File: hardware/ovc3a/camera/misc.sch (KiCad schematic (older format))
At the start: 2 parts, among them CON1 microSD_Card, U9 ARJ11C-MBSAS-A-BA-7MU2

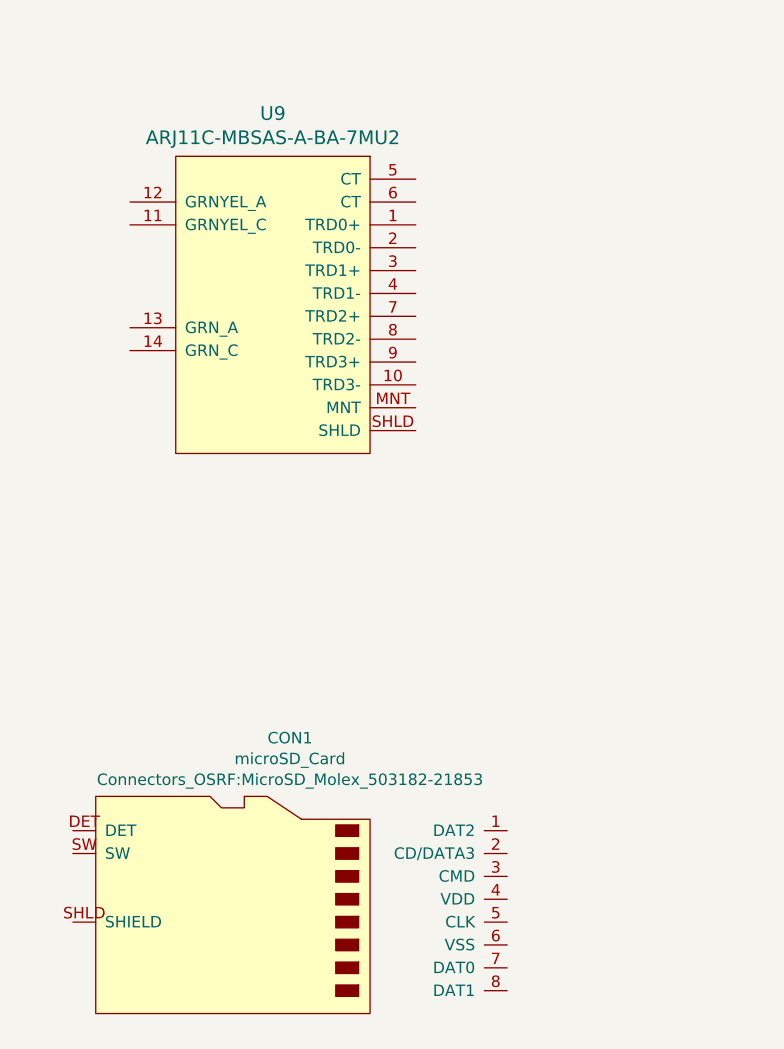
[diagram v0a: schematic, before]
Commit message: Shifted TE0820 module to make space for connectors, fixed library paths
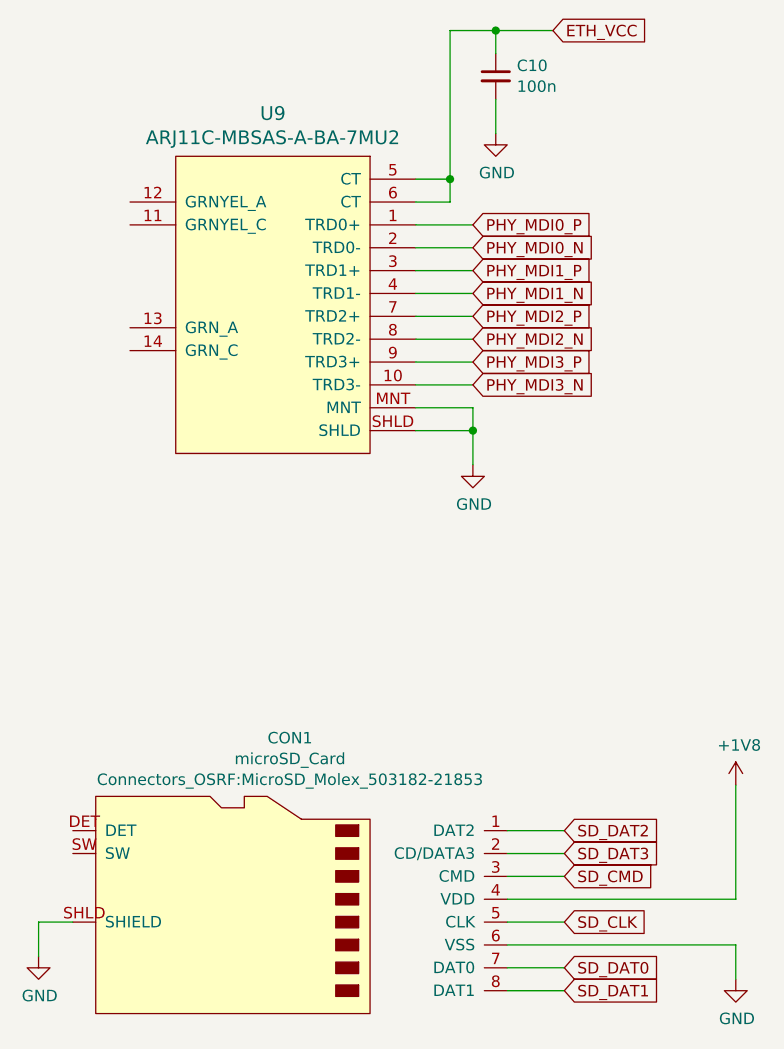
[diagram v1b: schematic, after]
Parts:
- added C10: 100n, Capacitor_SMD:C_0402_1005Metric, symbol Device:C_Small
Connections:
- net SD_DAT2: now reaches CON1.1 (DAT2)
- net SD_DAT3: now reaches CON1.2 (CD/DATA3)
- net SD_CMD: now reaches CON1.3 (CMD)
- net +1V8: now reaches CON1.4 (VDD)
- net SD_CLK: now reaches CON1.5 (CLK)
- net GND: now reaches CON1.6 (VSS)
- net GND: now also CON1.SHLD (SHIELD), U9.MNT, U9.SHLD, C10.2
- net SD_DAT0: now reaches CON1.7 (DAT0)
- net SD_DAT1: now reaches CON1.8 (DAT1)
- net PHY_MDI0_P: now reaches U9.1 (TRD0+)
- net PHY_MDI3_N: now reaches U9.10 (TRD3-)
- net PHY_MDI0_N: now reaches U9.2 (TRD0-)
- net PHY_MDI1_P: now reaches U9.3 (TRD1+)
- net PHY_MDI1_N: now reaches U9.4 (TRD1-)
- net ETH_VCC: now reaches U9.5 (CT)
- net ETH_VCC: now also U9.6 (CT), C10.1
- net PHY_MDI2_P: now reaches U9.7 (TRD2+)
- net PHY_MDI2_N: now reaches U9.8 (TRD2-)
- net PHY_MDI3_P: now reaches U9.9 (TRD3+)
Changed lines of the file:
@@
 	1    0    0    -1
 $EndComp
+Wire Wire Line
+	3050 1800 3300 1800
+Wire Wire Line
+	3300 1900 3050 1900
+Wire Wire Line
+	3300 2100 3050 2100
+Wire Wire Line
+	3050 2000 3300 2000
+Wire Wire Line
+	3300 2200 3050 2200
+Wire Wire Line
+	3050 2300 3300 2300
+Wire Wire Line
+	3300 2400 3050 2400
+Wire Wire Line
+	3050 2500 3300 2500
+$Comp
+L Device:C_Small C10
+U 1 1 5C4844F8
+P 3400 1150
+F 0 "C10" H 3492 1196 50  0000 L CNN
+F 1 "100n" H 3492 1105 50  0000 L CNN
+F 2 "Capacitor_SMD:C_0402_1005Metric" H 3400 1150 50  0001 C CNN
+F 3 "~" H 3400 1150 50  0001 C CNN
+	1    3400 1150
+	1    0    0    -1
+$EndComp
+Wire Wire Line
+	3050 1600 3200 1600
+Wire Wire Line
+	3200 1600 3200 950
+Wire Wire Line
+	3200 950  3400 950
+Wire Wire Line
+	3400 950  3400 1050
+Wire Wire Line
+	3050 1700 3200 1700
+Wire Wire Line
+	3200 1700 3200 1600
+Connection ~ 3200 1600
+$Comp
+L power:GND #PWR0115
+U 1 1 5C4874B9
+P 3400 1400
+F 0 "#PWR0115" H 3400 1150 50  0001 C CNN
+F 1 "GND" H 3405 1227 50  0000 C CNN
+F 2 "" H 3400 1400 50  0001 C CNN
+F 3 "" H 3400 1400 50  0001 C CNN
+	1    3400 1400
+	1    0    0    -1
+$EndComp
+$Comp
+L power:GND #PWR0116
+U 1 1 5C48A3ED
+P 3300 2850
+F 0 "#PWR0116" H 3300 2600 50  0001 C CNN
+F 1 "GND" H 3305 2677 50  0000 C CNN
+F 2 "" H 3300 2850 50  0001 C CNN
+F 3 "" H 3300 2850 50  0001 C CNN
+	1    3300 2850
+	1    0    0    -1
+$EndComp
+Wire Wire Line
+	3050 2700 3300 2700
+Wire Wire Line
+	3300 2700 3300 2850
+Wire Wire Line
+	3050 2600 3300 2600
+Wire Wire Line
+	3300 2600 3300 2700
+Connection ~ 3300 2700
+Wire Wire Line
+	3400 1400 3400 1250
+Wire Wire Line
+	3700 4450 3450 4450
+Wire Wire Line
+	3700 4550 3450 4550
+Wire Wire Line
+	3700 4650 3450 4650
+Wire Wire Line
+	3700 5150 3450 5150
+Wire Wire Line
+	3700 5050 3450 5050
+Wire Wire Line
+	3700 4850 3450 4850
+$Comp
+L power:GND #PWR0117
+U 1 1 5C49A0AD
+P 4450 5100
+F 0 "#PWR0117" H 4450 4850 50  0001 C CNN
+F 1 "GND" H 4455 4927 50  0000 C CNN
+F 2 "" H 4450 5100 50  0001 C CNN
+F 3 "" H 4450 5100 50  0001 C CNN
+	1    4450 5100
+	1    0    0    -1
+$EndComp
+Wire Wire Line
+	3450 4750 4450 4750
+Wire Wire Line
+	3450 4950 4450 4950
+Wire Wire Line
+	4450 4950 4450 5100
+$Comp
+L power:GND #PWR0119
+U 1 1 5C49BFA5
+P 1400 5000
+F 0 "#PWR0119" H 1400 4750 50  0001 C CNN
+F 1 "GND" H 1405 4827 50  0000 C CNN
+F 2 "" H 1400 5000 50  0001 C CNN
+F 3 "" H 1400 5000 50  0001 C CNN
+	1    1400 5000
+	1    0    0    -1
+$EndComp
+Wire Wire Line
+	1550 4850 1400 4850
+Wire Wire Line
+	1400 4850 1400 5000
+Wire Wire Line
+	4450 4250 4450 4750
+$Comp
+L power:+1V8 #PWR0118
+U 1 1 5C49AC58
+P 4450 4250
+F 0 "#PWR0118" H 4450 4100 50  0001 C CNN
+F 1 "+1V8" H 4465 4423 50  0000 C CNN
+F 2 "" H 4450 4250 50  0001 C CNN
+F 3 "" H 4450 4250 50  0001 C CNN
+	1    4450 4250
+	1    0    0    -1
+$EndComp
+Text GLabel 3700 4450 2    50   Input ~ 0
+SD_DAT2
+Text GLabel 3700 4550 2    50   Input ~ 0
+SD_DAT3
+Text GLabel 3700 4650 2    50   Input ~ 0
+SD_CMD
+Text GLabel 3700 4850 2    50   Input ~ 0
+SD_CLK
+Text GLabel 3700 5050 2    50   Input ~ 0
+SD_DAT0
+Text GLabel 3700 5150 2    50   Input ~ 0
+SD_DAT1
+Text GLabel 3300 1800 2    50   Input ~ 0
+PHY_MDI0_P
+Text GLabel 3300 1900 2    50   Input ~ 0
+PHY_MDI0_N
+Text GLabel 3300 2000 2    50   Input ~ 0
+PHY_MDI1_P
+Text GLabel 3300 2100 2    50   Input ~ 0
+PHY_MDI1_N
+Text GLabel 3300 2200 2    50   Input ~ 0
+PHY_MDI2_P
+Text GLabel 3300 2300 2    50   Input ~ 0
+PHY_MDI2_N
+Text GLabel 3300 2400 2    50   Input ~ 0
+PHY_MDI3_P
+Text GLabel 3300 2500 2    50   Input ~ 0
+PHY_MDI3_N
+Text GLabel 3650 950  2    50   Input ~ 0
+ETH_VCC
+Wire Wire Line
+	3650 950  3400 950
+Connection ~ 3400 950
 $EndSCHEMATC

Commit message: Fixed SD power to 3.3V
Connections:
- net +1V8 renamed +3V3
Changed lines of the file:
@@
 Wire Wire Line
 	4450 4250 4450 4750
-$Comp
-L power:+1V8 #PWR0118
-U 1 1 5C49AC58
-P 4450 4250
-F 0 "#PWR0118" H 4450 4100 50  0001 C CNN
-F 1 "+1V8" H 4465 4423 50  0000 C CNN
-F 2 "" H 4450 4250 50  0001 C CNN
-F 3 "" H 4450 4250 50  0001 C CNN
-	1    4450 4250
-	1    0    0    -1
-$EndComp
 Text GLabel 3700 4450 2    50   Input ~ 0
 SD_DAT2
@@
 	3650 950  3400 950
 Connection ~ 3400 950
+$Comp
+L power:+3.3V #PWR?
+U 1 1 5C4E6A5A
+P 4450 4250
+F 0 "#PWR?" H 4450 4100 50  0001 C CNN
+F 1 "+3.3V" H 4465 4423 50  0000 C CNN
+F 2 "" H 4450 4250 50  0001 C CNN
+F 3 "" H 4450 4250 50  0001 C CNN
+	1    4450 4250
+	1    0    0    -1
+$EndComp
 $EndSCHEMATC

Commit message: Preliminary component placement
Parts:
- added J5: Conn_02x15_Odd_Even, Connector_PinHeader_2.00mm:PinHeader_2x15_P2.00mm_Vertical, symbol Connector_Generic:Conn_02x15_Odd_Even
- added R12, R13: 220R, Resistor_SMD:R_0603_1608Metric, symbol Device:R_Small
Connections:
- net +3V3: now also J5.1 (Pin_1), J5.2 (Pin_2)
- net GND: now also U9.11 (GRNYEL_C), U9.14 (GRN_C), J5.17 (Pin_17), J5.18 (Pin_18), J5.29 (Pin_29), J5.30 (Pin_30), J5.5 (Pin_5), J5.6 (Pin_6)
- net at U9.12 (GRNYEL_A): now also R12.1
- net at U9.13 (GRN_A): now also R13.1
- new net +1V8: J5.3 (Pin_3), J5.4 (Pin_4)
- new net LED_L: R13.2
- new net LED_R: R12.2
- new net PGOOD: J5.7 (Pin_7)
- new net SPI_CLK: J5.25 (Pin_25)
- new net SPI_MISO: J5.26 (Pin_26)
- new net SPI_MOSI: J5.28 (Pin_28)
- new net SPI_SS1: J5.27 (Pin_27)
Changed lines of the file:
@@
 Connection ~ 3400 950
 $Comp
-L power:+3.3V #PWR?
+L power:+3.3V #PWR0118
 U 1 1 5C4E6A5A
 P 4450 4250
-F 0 "#PWR?" H 4450 4100 50  0001 C CNN
+F 0 "#PWR0118" H 4450 4100 50  0001 C CNN
 F 1 "+3.3V" H 4465 4423 50  0000 C CNN
 F 2 "" H 4450 4250 50  0001 C CNN
@@
 	1    0    0    -1
 $EndComp
+$Comp
+L Device:R_Small R13
+U 1 1 5C4E7858
+P 1500 2250
+F 0 "R13" V 1304 2250 50  0000 C CNN
+F 1 "220R" V 1395 2250 50  0000 C CNN
+F 2 "Resistor_SMD:R_0603_1608Metric" H 1500 2250 50  0001 C CNN
+F 3 "~" H 1500 2250 50  0001 C CNN
+	1    1500 2250
+	0    1    1    0
+$EndComp
+Wire Wire Line
+	1800 2250 1600 2250
+$Comp
+L power:GND #PWR0120
+U 1 1 5C4E8986
+P 1700 2500
+F 0 "#PWR0120" H 1700 2250 50  0001 C CNN
+F 1 "GND" H 1705 2327 50  0000 C CNN
+F 2 "" H 1700 2500 50  0001 C CNN
+F 3 "" H 1700 2500 50  0001 C CNN
+	1    1700 2500
+	1    0    0    -1
+$EndComp
+Wire Wire Line
+	1800 2350 1700 2350
+Wire Wire Line
+	1700 2350 1700 2500
+Text GLabel 1200 2250 0    50   Input ~ 0
+LED_L
+Wire Wire Line
+	1200 2250 1400 2250
+$Comp
+L Device:R_Small R12
+U 1 1 5C4EAD2A
+P 1500 1700
+F 0 "R12" V 1304 1700 50  0000 C CNN
+F 1 "220R" V 1395 1700 50  0000 C CNN
+F 2 "Resistor_SMD:R_0603_1608Metric" H 1500 1700 50  0001 C CNN
+F 3 "~" H 1500 1700 50  0001 C CNN
+	1    1500 1700
+	0    1    1    0
+$EndComp
+Wire Wire Line
+	1800 1700 1600 1700
+$Comp
+L power:GND #PWR0131
+U 1 1 5C4EAD31
+P 1700 1950
+F 0 "#PWR0131" H 1700 1700 50  0001 C CNN
+F 1 "GND" H 1705 1777 50  0000 C CNN
+F 2 "" H 1700 1950 50  0001 C CNN
+F 3 "" H 1700 1950 50  0001 C CNN
+	1    1700 1950
+	1    0    0    -1
+$EndComp
+Wire Wire Line
+	1800 1800 1700 1800
+Wire Wire Line
+	1700 1800 1700 1950
+Text GLabel 1200 1700 0    50   Input ~ 0
+LED_R
+Wire Wire Line
+	1200 1700 1400 1700
+$Comp
+L Connector_Generic:Conn_02x15_Odd_Even J5
+U 1 1 5C4F53CA
+P 6900 2550
+F 0 "J5" H 6950 3467 50  0000 C CNN
+F 1 "Conn_02x15_Odd_Even" H 6950 3376 50  0000 C CNN
+F 2 "Connector_PinHeader_2.00mm:PinHeader_2x15_P2.00mm_Vertical" H 6900 2550 50  0001 C CNN
+F 3 "~" H 6900 2550 50  0001 C CNN
+	1    6900 2550
+	1    0    0    -1
+$EndComp
+$Comp
+L power:+3.3V #PWR0138
+U 1 1 5C51EADE
+P 6450 1550
+F 0 "#PWR0138" H 6450 1400 50  0001 C CNN
+F 1 "+3.3V" H 6465 1723 50  0000 C CNN
+F 2 "" H 6450 1550 50  0001 C CNN
+F 3 "" H 6450 1550 50  0001 C CNN
+	1    6450 1550
+	1    0    0    -1
+$EndComp
+$Comp
+L power:+3.3V #PWR0139
+U 1 1 5C51EDE5
+P 7450 1550
+F 0 "#PWR0139" H 7450 1400 50  0001 C CNN
+F 1 "+3.3V" H 7465 1723 50  0000 C CNN
+F 2 "" H 7450 1550 50  0001 C CNN
+F 3 "" H 7450 1550 50  0001 C CNN
+	1    7450 1550
+	1    0    0    -1
+$EndComp
+Wire Wire Line
+	7450 1850 7450 1550
+Wire Wire Line
+	6450 1850 6450 1550
+$Comp
+L power:+1V8 #PWR0140
+U 1 1 5C522639
+P 6150 1450
+F 0 "#PWR0140" H 6150 1300 50  0001 C CNN
+F 1 "+1V8" H 6165 1623 50  0000 C CNN
+F 2 "" H 6150 1450 50  0001 C CNN
+F 3 "" H 6150 1450 50  0001 C CNN
+	1    6150 1450
+	1    0    0    -1
+$EndComp
+$Comp
+L power:+1V8 #PWR0141
+U 1 1 5C522CA8
+P 7750 1450
+F 0 "#PWR0141" H 7750 1300 50  0001 C CNN
+F 1 "+1V8" H 7765 1623 50  0000 C CNN
+F 2 "" H 7750 1450 50  0001 C CNN
+F 3 "" H 7750 1450 50  0001 C CNN
+	1    7750 1450
+	1    0    0    -1
+$EndComp
+Wire Wire Line
+	7200 1950 7750 1950
+Wire Wire Line
+	7750 1950 7750 1450
+Wire Wire Line
+	6700 1950 6150 1950
+Wire Wire Line
+	6150 1950 6150 1450
+$Comp
+L power:GND #PWR0143
+U 1 1 5C52693D
+P 6650 3400
+F 0 "#PWR0143" H 6650 3150 50  0001 C CNN
+F 1 "GND" H 6655 3227 50  0000 C CNN
+F 2 "" H 6650 3400 50  0001 C CNN
+F 3 "" H 6650 3400 50  0001 C CNN
+	1    6650 3400
+	1    0    0    -1
+$EndComp
+Text GLabel 6500 2150 0    50   Input ~ 0
+PGOOD
+Text GLabel 6500 3150 0    50   Input ~ 0
+SPI_SS1
+Text GLabel 6500 3050 0    50   Input ~ 0
+SPI_CLK
+Text GLabel 7400 3150 2    50   Input ~ 0
+SPI_MOSI
+Text GLabel 7400 3050 2    50   Input ~ 0
+SPI_MISO
+Wire Wire Line
+	6650 2050 6650 2650
+Wire Wire Line
+	6650 2050 6700 2050
+Wire Wire Line
+	6700 2650 6650 2650
+Connection ~ 6650 2650
+Wire Wire Line
+	6650 2650 6650 3250
+Wire Wire Line
+	6700 3250 6650 3250
+Connection ~ 6650 3250
+Wire Wire Line
+	6650 3250 6650 3400
+Wire Wire Line
+	7250 2050 7250 2650
+$Comp
+L power:GND #PWR0142
+U 1 1 5C52535B
+P 7250 3400
+F 0 "#PWR0142" H 7250 3150 50  0001 C CNN
+F 1 "GND" H 7255 3227 50  0000 C CNN
+F 2 "" H 7250 3400 50  0001 C CNN
+F 3 "" H 7250 3400 50  0001 C CNN
+	1    7250 3400
+	1    0    0    -1
+$EndComp
+Wire Wire Line
+	7200 3250 7250 3250
+Connection ~ 7250 3250
+Wire Wire Line
+	7250 3250 7250 3400
+Wire Wire Line
+	7200 2650 7250 2650
+Connection ~ 7250 2650
+Wire Wire Line
+	7250 2650 7250 3250
+Wire Wire Line
+	7200 2050 7250 2050
+Wire Wire Line
+	6700 2150 6500 2150
+Wire Wire Line
+	7400 3050 7200 3050
+Wire Wire Line
+	7200 3150 7400 3150
+Wire Wire Line
+	6500 3050 6700 3050
+Wire Wire Line
+	6700 3150 6500 3150
+Wire Wire Line
+	6700 1850 6450 1850
+Wire Wire Line
+	7450 1850 7200 1850
 $EndSCHEMATC

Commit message: Placement completed, pre FPGA IO assignment
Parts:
- added D1, D2: LED, LED_SMD:LED_0402_1005Metric, symbol Device:LED
- added J6: Conn_02x04_Counter_Clockwise, Connector_PinSocket_2.00mm:PinSocket_2x04_P2.00mm_Vertical, symbol Connector_Generic:Conn_02x04_Odd_Even
- added R14, R15: 220R, Resistor_SMD:R_0603_1608Metric, symbol Device:R_Small
- J5: footprint Connector_PinHeader_2.00mm:PinHeader_2x15_P2.00mm_Vertical -> Connector_PinSocket_2.00mm:PinSocket_2x15_P2.00mm_Vertical
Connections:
- net +3V3: now also J6.1 (Pin_1)
- net GND: now also D1.1 (K), D2.1 (K), J6.7 (Pin_7), J6.8 (Pin_8)
- net GPIO2: now reaches J5.10 (Pin_10)
- net GPIO3: now reaches J5.11 (Pin_11)
- net GPIO4: now reaches J5.12 (Pin_12)
- net GPIO5: now reaches J5.13 (Pin_13)
- net GPIO6: now reaches J5.14 (Pin_14)
- net GPIO7: now reaches J5.15 (Pin_15)
- net GPIO8: now reaches J5.16 (Pin_16)
- net GPIO9: now reaches J5.19 (Pin_19)
- net GPIO10: now reaches J5.20 (Pin_20)
- net GPIO11: now reaches J5.21 (Pin_21)
- net GPIO12: now reaches J5.22 (Pin_22)
- net GPIO13: now reaches J5.23 (Pin_23)
- net GPIO14: now reaches J5.24 (Pin_24)
- net GPIO0: now reaches J5.8 (Pin_8)
- net GPIO1: now reaches J5.9 (Pin_9)
- net LED_L renamed ETH_LED_L
- net LED_R renamed ETH_LED_R
- net SPI_CLK renamed GPIO15
- net SPI_MISO renamed GPIO16
- net SPI_MOSI renamed GPIO18
- net SPI_SS1 renamed GPIO17
- new net: D1.2 (A), R14.1
- new net: D2.2 (A), R15.1
- new net JTAG_HALT: J6.2 (Pin_2)
- new net JTAG_TCK: J6.4 (Pin_4)
- new net JTAG_TDI: J6.5 (Pin_5)
- new net JTAG_TDO: J6.6 (Pin_6)
- new net JTAG_TMS: J6.3 (Pin_3)
- new net LED0: R14.2
- new net LED1: R15.2
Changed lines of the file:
@@
 	1700 2350 1700 2500
 Text GLabel 1200 2250 0    50   Input ~ 0
-LED_L
+ETH_LED_L
 Wire Wire Line
 	1200 2250 1400 2250
@@
 	1700 1800 1700 1950
 Text GLabel 1200 1700 0    50   Input ~ 0
-LED_R
+ETH_LED_R
 Wire Wire Line
 	1200 1700 1400 1700
@@
 F 0 "J5" H 6950 3467 50  0000 C CNN
 F 1 "Conn_02x15_Odd_Even" H 6950 3376 50  0000 C CNN
-F 2 "Connector_PinHeader_2.00mm:PinHeader_2x15_P2.00mm_Vertical" H 6900 2550 50  0001 C CNN
+F 2 "Connector_PinSocket_2.00mm:PinSocket_2x15_P2.00mm_Vertical" H 6900 2550 50  0001 C CNN
 F 3 "~" H 6900 2550 50  0001 C CNN
 	1    6900 2550
@@
 Text GLabel 6500 2150 0    50   Input ~ 0
 PGOOD
-Text GLabel 6500 3150 0    50   Input ~ 0
-SPI_SS1
-Text GLabel 6500 3050 0    50   Input ~ 0
-SPI_CLK
-Text GLabel 7400 3150 2    50   Input ~ 0
-SPI_MOSI
-Text GLabel 7400 3050 2    50   Input ~ 0
-SPI_MISO
 Wire Wire Line
 	6650 2050 6650 2650
@@
 	6700 2150 6500 2150
 Wire Wire Line
+	6700 1850 6450 1850
+Wire Wire Line
+	7450 1850 7200 1850
+$Comp
+L Connector_Generic:Conn_02x04_Odd_Even J6
+U 1 1 5E9E978B
+P 7000 4750
+F 0 "J6" H 7100 5100 50  0000 C CNN
+F 1 "Conn_02x04_Counter_Clockwise" H 7400 5000 50  0000 C CNN
+F 2 "Connector_PinSocket_2.00mm:PinSocket_2x04_P2.00mm_Vertical" H 7000 4750 50  0001 C CNN
+F 3 "~" H 7000 4750 50  0001 C CNN
+	1    7000 4750
+	1    0    0    -1
+$EndComp
+$Comp
+L power:GND #PWR0167
+U 1 1 5E9EB5DC
+P 7050 5150
+F 0 "#PWR0167" H 7050 4900 50  0001 C CNN
+F 1 "GND" H 7055 4977 50  0000 C CNN
+F 2 "" H 7050 5150 50  0001 C CNN
+F 3 "" H 7050 5150 50  0001 C CNN
+	1    7050 5150
+	1    0    0    -1
+$EndComp
+Wire Wire Line
+	7300 4950 7300 5100
+Wire Wire Line
+	7300 5100 7050 5100
+Wire Wire Line
+	7050 5150 7050 5100
+Connection ~ 7050 5100
+Wire Wire Line
+	7050 5100 6800 5100
+Wire Wire Line
+	6800 4950 6800 5100
+Text GLabel 6700 4750 0    50   Input ~ 0
+JTAG_TMS
+Text GLabel 6700 4850 0    50   Input ~ 0
+JTAG_TDI
+Text GLabel 7400 4850 2    50   Input ~ 0
+JTAG_TDO
+Text GLabel 7400 4750 2    50   Input ~ 0
+JTAG_TCK
+Wire Wire Line
+	7400 4750 7300 4750
+Wire Wire Line
+	7400 4850 7300 4850
+Wire Wire Line
+	6800 4750 6700 4750
+Wire Wire Line
+	6800 4850 6700 4850
+$Comp
+L power:+3.3V #PWR0182
+U 1 1 5EA225E7
+P 6700 4400
+F 0 "#PWR0182" H 6700 4250 50  0001 C CNN
+F 1 "+3.3V" H 6715 4573 50  0000 C CNN
+F 2 "" H 6700 4400 50  0001 C CNN
+F 3 "" H 6700 4400 50  0001 C CNN
+	1    6700 4400
+	1    0    0    -1
+$EndComp
+Wire Wire Line
+	6800 4650 6700 4650
+Wire Wire Line
+	6700 4650 6700 4400
+Text GLabel 7400 4650 2    50   Input ~ 0
+JTAG_HALT
+Wire Wire Line
+	7400 4650 7300 4650
+$Comp
+L Device:LED D1
+U 1 1 5EA32365
+P 5850 5650
+F 0 "D1" H 5843 5395 50  0000 C CNN
+F 1 "LED" H 5843 5486 50  0000 C CNN
+F 2 "LED_SMD:LED_0402_1005Metric" H 5850 5650 50  0001 C CNN
+F 3 "~" H 5850 5650 50  0001 C CNN
+	1    5850 5650
+	-1   0    0    1
+$EndComp
+$Comp
+L Device:LED D2
+U 1 1 5EA38CC0
+P 5850 6100
+F 0 "D2" H 5843 5845 50  0000 C CNN
+F 1 "LED" H 5843 5936 50  0000 C CNN
+F 2 "LED_SMD:LED_0402_1005Metric" H 5850 6100 50  0001 C CNN
+F 3 "~" H 5850 6100 50  0001 C CNN
+	1    5850 6100
+	-1   0    0    1
+$EndComp
+$Comp
+L power:GND #PWR0183
+U 1 1 5EA39EBE
+P 6150 6250
+F 0 "#PWR0183" H 6150 6000 50  0001 C CNN
+F 1 "GND" H 6155 6077 50  0000 C CNN
+F 2 "" H 6150 6250 50  0001 C CNN
+F 3 "" H 6150 6250 50  0001 C CNN
+	1    6150 6250
+	1    0    0    -1
+$EndComp
+Wire Wire Line
+	6000 6100 6150 6100
+Wire Wire Line
+	6150 6100 6150 6250
+Wire Wire Line
+	6000 5650 6150 5650
+Wire Wire Line
+	6150 5650 6150 6100
+Connection ~ 6150 6100
+$Comp
+L Device:R_Small R14
+U 1 1 5EA3E3D8
+P 5450 5650
+F 0 "R14" V 5254 5650 50  0000 C CNN
+F 1 "220R" V 5345 5650 50  0000 C CNN
+F 2 "Resistor_SMD:R_0603_1608Metric" H 5450 5650 50  0001 C CNN
+F 3 "~" H 5450 5650 50  0001 C CNN
+	1    5450 5650
+	0    1    1    0
+$EndComp
+$Comp
+L Device:R_Small R15
+U 1 1 5EA3ED75
+P 5450 6100
+F 0 "R15" V 5254 6100 50  0000 C CNN
+F 1 "220R" V 5345 6100 50  0000 C CNN
+F 2 "Resistor_SMD:R_0603_1608Metric" H 5450 6100 50  0001 C CNN
+F 3 "~" H 5450 6100 50  0001 C CNN
+	1    5450 6100
+	0    1    1    0
+$EndComp
+Wire Wire Line
+	5550 6100 5700 6100
+Wire Wire Line
+	5550 5650 5700 5650
+Text GLabel 5150 5650 0    50   Input ~ 0
+LED0
+Text GLabel 5150 6100 0    50   Input ~ 0
+LED1
+Wire Wire Line
+	5150 5650 5350 5650
+Wire Wire Line
+	5350 6100 5150 6100
+Wire Wire Line
+	6500 2250 6700 2250
+Text GLabel 6500 2350 0    50   Input ~ 0
+GPIO3
+Wire Wire Line
+	6500 2350 6700 2350
+Text GLabel 6500 2450 0    50   Input ~ 0
+GPIO5
+Wire Wire Line
+	6500 2450 6700 2450
+Text GLabel 6500 2550 0    50   Input ~ 0
+GPIO7
+Wire Wire Line
+	6500 2550 6700 2550
+Text GLabel 6500 2750 0    50   Input ~ 0
+GPIO9
+Wire Wire Line
+	6500 2750 6700 2750
+Text GLabel 6500 2850 0    50   Input ~ 0
+GPIO11
+Wire Wire Line
+	6500 2850 6700 2850
+Wire Wire Line
+	6500 2950 6700 2950
+Wire Wire Line
+	6500 3050 6700 3050
+Wire Wire Line
+	6500 3150 6700 3150
+Text GLabel 7400 2150 2    50   Input ~ 0
+GPIO0
+Wire Wire Line
+	7400 2150 7200 2150
+Text GLabel 7400 2250 2    50   Input ~ 0
+GPIO2
+Wire Wire Line
+	7400 2250 7200 2250
+Text GLabel 7400 2350 2    50   Input ~ 0
+GPIO4
+Wire Wire Line
+	7400 2350 7200 2350
+Text GLabel 7400 2450 2    50   Input ~ 0
+GPIO6
+Wire Wire Line
+	7400 2450 7200 2450
+Text GLabel 7400 2550 2    50   Input ~ 0
+GPIO8
+Wire Wire Line
+	7400 2550 7200 2550
+Text GLabel 7400 2750 2    50   Input ~ 0
+GPIO10
+Wire Wire Line
+	7400 2750 7200 2750
+Wire Wire Line
+	7400 2850 7200 2850
+Wire Wire Line
+	7400 2950 7200 2950
+Wire Wire Line
 	7400 3050 7200 3050
 Wire Wire Line
-	7200 3150 7400 3150
-Wire Wire Line
-	6500 3050 6700 3050
-Wire Wire Line
-	6700 3150 6500 3150
-Wire Wire Line
-	6700 1850 6450 1850
-Wire Wire Line
-	7450 1850 7200 1850
+	7400 3150 7200 3150
+Text GLabel 6500 2250 0    50   Input ~ 0
+GPIO1
+Text GLabel 6500 2950 0    50   Input ~ 0
+GPIO13
+Text GLabel 6500 3050 0    50   Input ~ 0
+GPIO15
+Text GLabel 6500 3150 0    50   Input ~ 0
+GPIO17
+Text GLabel 7400 2850 2    50   Input ~ 0
+GPIO12
+Text GLabel 7400 2950 2    50   Input ~ 0
+GPIO14
+Text GLabel 7400 3050 2    50   Input ~ 0
+GPIO16
+Text GLabel 7400 3150 2    50   Input ~ 0
+GPIO18
 $EndSCHEMATC
